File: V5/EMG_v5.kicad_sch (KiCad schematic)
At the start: 20 parts, among them J1 SJ1-3523N, J2 Output, U1 INA333xxDGK, U2 MCP6002-xP

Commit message: add power reference schematic block
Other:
- added sheet POWER_REFERENCE_BLOCK (POWER_REFERENCE_BLOCK.kicad_sch)
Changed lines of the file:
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@@
 		)
 		(instances
-			(project "EMG_v4"
+			(project "EMG_v5"
 				(path "/2c477672-822a-487d-bb83-204f5f41dbd8"
 					(reference "#PWR02")
@@
 		)
 		(instances
-			(project "EMG_v4"
+			(project "EMG_v5"
 				(path "/2c477672-822a-487d-bb83-204f5f41dbd8"
 					(reference "R6")
@@
 		)
 		(instances
-			(project "EMG_v4"
+			(project "EMG_v5"
 				(path "/2c477672-822a-487d-bb83-204f5f41dbd8"
 					(reference "R5")
@@
 		)
 		(instances
-			(project "EMG_v4"
+			(project "EMG_v5"
 				(path "/2c477672-822a-487d-bb83-204f5f41dbd8"
 					(reference "U2")
@@
 		)
 		(instances
-			(project "EMG_v4"
+			(project "EMG_v5"
 				(path "/2c477672-822a-487d-bb83-204f5f41dbd8"
 					(reference "Rg1")
@@
 		)
 		(instances
-			(project "EMG_v4"
+			(project "EMG_v5"
 				(path "/2c477672-822a-487d-bb83-204f5f41dbd8"
 					(reference "C2")
@@
 		)
 		(instances
-			(project "EMG_v4"
+			(project "EMG_v5"
 				(path "/2c477672-822a-487d-bb83-204f5f41dbd8"
 					(reference "R8")
@@
 		)
 		(instances
-			(project "EMG_v4"
+			(project "EMG_v5"
 				(path "/2c477672-822a-487d-bb83-204f5f41dbd8"
 					(reference "R3")
@@
 		)
 		(instances
-			(project "EMG_v4"
+			(project "EMG_v5"
 				(path "/2c477672-822a-487d-bb83-204f5f41dbd8"
 					(reference "R7")
@@
 		)
 		(instances
-			(project "EMG_v4"
+			(project "EMG_v5"
 				(path "/2c477672-822a-487d-bb83-204f5f41dbd8"
 					(reference "#FLG01")
@@
 		)
 		(instances
-			(project "EMG_v4"
+			(project "EMG_v5"
 				(path "/2c477672-822a-487d-bb83-204f5f41dbd8"
 					(reference "R2")
@@
 		)
 		(instances
-			(project "EMG_v4"
+			(project "EMG_v5"
 				(path "/2c477672-822a-487d-bb83-204f5f41dbd8"
 					(reference "U2")
@@
 		)
 		(instances
-			(project "EMG_v4"
+			(project "EMG_v5"
 				(path "/2c477672-822a-487d-bb83-204f5f41dbd8"
 					(reference "C6")
@@
 		)
 		(instances
-			(project "EMG_v4"
+			(project "EMG_v5"
 				(path "/2c477672-822a-487d-bb83-204f5f41dbd8"
 					(reference "R4")
@@
 		)
 		(instances
-			(project "EMG_v4"
+			(project "EMG_v5"
 				(path "/2c477672-822a-487d-bb83-204f5f41dbd8"
 					(reference "Rf1")
@@
 		)
 		(instances
-			(project "EMG_v4"
+			(project "EMG_v5"
 				(path "/2c477672-822a-487d-bb83-204f5f41dbd8"
 					(reference "#PWR01")
@@
 		)
 		(instances
-			(project "EMG_v4"
+			(project "EMG_v5"
 				(path "/2c477672-822a-487d-bb83-204f5f41dbd8"
 					(reference "J1")
@@
 		)
 		(instances
-			(project "EMG_v4"
+			(project "EMG_v5"
 				(path "/2c477672-822a-487d-bb83-204f5f41dbd8"
 					(reference "J2")
@@
 		)
 		(instances
-			(project "EMG_v4"
+			(project "EMG_v5"
 				(path "/2c477672-822a-487d-bb83-204f5f41dbd8"
 					(reference "C3")
@@
 		)
 		(instances
-			(project "EMG_v4"
+			(project "EMG_v5"
 				(path "/2c477672-822a-487d-bb83-204f5f41dbd8"
 					(reference "Cf2")
@@
 		)
 		(instances
-			(project "EMG_v4"
+			(project "EMG_v5"
 				(path "/2c477672-822a-487d-bb83-204f5f41dbd8"
 					(reference "U2")
@@
 		)
 		(instances
-			(project "EMG_v4"
+			(project "EMG_v5"
 				(path "/2c477672-822a-487d-bb83-204f5f41dbd8"
 					(reference "C4")
@@
 		)
 		(instances
-			(project "EMG_v4"
+			(project "EMG_v5"
 				(path "/2c477672-822a-487d-bb83-204f5f41dbd8"
 					(reference "C5")
@@
 		)
 		(instances
-			(project "EMG_v4"
+			(project "EMG_v5"
 				(path "/2c477672-822a-487d-bb83-204f5f41dbd8"
 					(reference "U1")
@@
 		)
 		(instances
-			(project "EMG_v4"
+			(project "EMG_v5"
 				(path "/2c477672-822a-487d-bb83-204f5f41dbd8"
 					(reference "Rg_HPF1")
@@
 		)
 		(instances
-			(project "EMG_v4"
+			(project "EMG_v5"
 				(path "/2c477672-822a-487d-bb83-204f5f41dbd8"
 					(reference "#FLG02")
@@
 				)
 			)
+		)
+	)
+	(sheet
+		(at 146.05 101.6)
+		(size 45.72 25.4)
+		(exclude_from_sim no)
+		(in_bom yes)
+		(on_board yes)
+		(dnp no)
+		(fields_autoplaced yes)
+		(stroke
+			(width 0.1524)
+			(type solid)
+		)
+		(fill
+			(color 0 0 0 0)
+		)
+		(property "Sheetname" "POWER_REFERENCE_BLOCK"
+			(at 146.05 100.8888 0)
+			(show_name no)
+			(do_not_autoplace no)
+			(effects
+				(font
+					(size 1.27 1.27)
+				)
+				(justify left bottom)
+			)
+		)
+		(property "Sheetfile" "POWER_REFERENCE_BLOCK.kicad_sch"
+			(at 146.05 127.6096 0)
+			(show_name no)
+			(do_not_autoplace no)
+			(effects
+				(font
+					(size 1.27 1.27)
+				)
+				(justify left top)
+			)
+		)
+		(instances
+			(project "EMG_v5"
+				(path "/4b7d3b9f-6eb5-4b2b-a72d-ec3d44a09101"
+					(page "2")
+				)
+			)

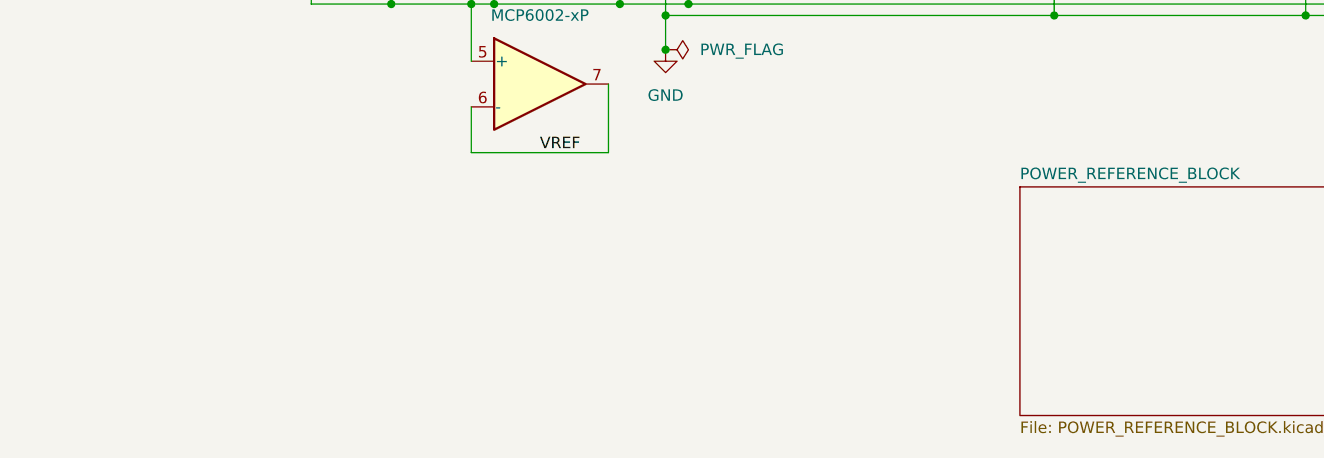
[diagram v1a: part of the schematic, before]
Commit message: add channel 1 analog schematic candidate
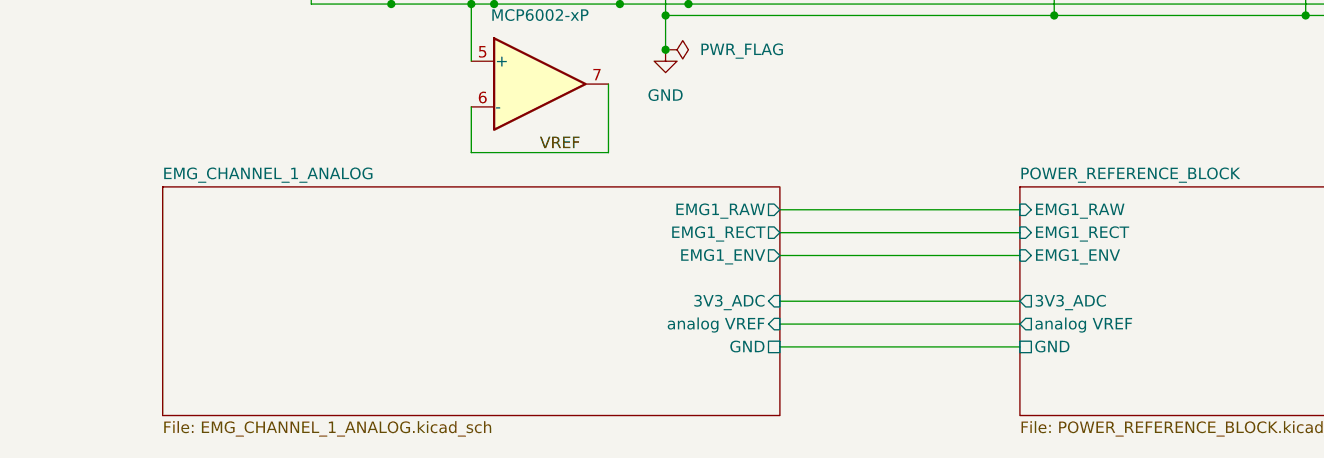
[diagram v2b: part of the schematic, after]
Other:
- added sheet EMG_CHANNEL_1_ANALOG (EMG_CHANNEL_1_ANALOG.kicad_sch)
- sheet POWER_REFERENCE_BLOCK ports: added 3V3_ADC, EMG1_ENV, EMG1_RAW, EMG1_RECT, GND, analog VREF; removed none
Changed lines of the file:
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@@
+			)
+		)
+		(pin "EMG1_RAW" input
+			(at 146.05 104.14 180)
+			(effects
+				(font
+					(size 1.27 1.27)
+				)
+				(justify left)
+			)
+		)
+		(pin "EMG1_RECT" input
+			(at 146.05 106.68 180)
+			(effects
+				(font
+					(size 1.27 1.27)
+				)
+				(justify left)
+			)
+		)
+		(pin "EMG1_ENV" input
+			(at 146.05 109.22 180)
+			(effects
+				(font
+					(size 1.27 1.27)
+				)
+				(justify left)
+			)
+		)
+		(pin "3V3_ADC" output
+			(at 146.05 114.3 180)
+			(effects
+				(font
+					(size 1.27 1.27)
+				)
+				(justify left)
+			)
+		)
+		(pin "analog VREF" output
+			(at 146.05 116.84 180)
+			(effects
+				(font
+					(size 1.27 1.27)
+				)
+				(justify left)
+			)
+		)
+		(pin "GND" passive
+			(at 146.05 119.38 180)
+			(effects
+				(font
+					(size 1.27 1.27)
+				)
+				(justify left)
 			)
 		)
@@
 				)
 			)
+		)
+	)
+	(wire
+		(pts
+			(xy 119.38 104.14) (xy 146.05 104.14)
+		)
+		(stroke
+			(width 0)
+			(type default)
+		)
+	)
+	(wire
+		(pts
+			(xy 119.38 106.68) (xy 146.05 106.68)
+		)
+		(stroke
+			(width 0)
+			(type default)
+		)
+	)
+	(wire
+		(pts
+			(xy 119.38 109.22) (xy 146.05 109.22)
+		)
+		(stroke
+			(width 0)
+			(type default)
+		)
+	)
+	(wire
+		(pts
+			(xy 119.38 114.3) (xy 146.05 114.3)
+		)
+		(stroke
+			(width 0)
+			(type default)
+		)
+	)
+	(wire
+		(pts
+			(xy 119.38 116.84) (xy 146.05 116.84)
+		)
+		(stroke
+			(width 0)
+			(type default)
+		)
+	)
+	(wire
+		(pts
+			(xy 119.38 119.38) (xy 146.05 119.38)
+		)
+		(stroke
+			(width 0)
+			(type default)
+		)
+	)
+	(sheet
+		(at 50.8 101.6)
+		(size 68.58 25.4)
+		(exclude_from_sim no)
+		(in_bom yes)
+		(on_board yes)
+		(dnp no)
+		(fields_autoplaced yes)
+		(stroke
+			(width 0.1524)
+			(type solid)
+		)
+		(fill
+			(color 0 0 0 0)
+		)
+		(property "Sheetname" "EMG_CHANNEL_1_ANALOG"
+			(at 50.8 100.8888 0)
+			(show_name no)
+			(do_not_autoplace no)
+			(effects
+				(font
+					(size 1.27 1.27)
+				)
+				(justify left bottom)
+			)
+		)
+		(property "Sheetfile" "EMG_CHANNEL_1_ANALOG.kicad_sch"
+			(at 50.8 127.6096 0)
+			(show_name no)
+			(do_not_autoplace no)
+			(effects
+				(font
+					(size 1.27 1.27)
+				)
+				(justify left top)
+			)
+		)
+		(pin "EMG1_RAW" output
+			(at 119.38 104.14 0)
+			(effects
+				(font
+					(size 1.27 1.27)
+				)
+				(justify right)
+			)
+		)
+		(pin "EMG1_RECT" output
+			(at 119.38 106.68 0)
+			(effects
+				(font
+					(size 1.27 1.27)
+				)
+				(justify right)
+			)
+		)
+		(pin "EMG1_ENV" output
+			(at 119.38 109.22 0)
+			(effects
+				(font
+					(size 1.27 1.27)
+				)
+				(justify right)
+			)
+		)
+		(pin "3V3_ADC" input
+			(at 119.38 114.3 0)
+			(effects
+				(font
+					(size 1.27 1.27)
+				)
+				(justify right)
+			)
+		)
+		(pin "analog VREF" input
+			(at 119.38 116.84 0)
+			(effects
+				(font
+					(size 1.27 1.27)
+				)
+				(justify right)
+			)
+		)
+		(pin "GND" passive
+			(at 119.38 119.38 0)
+			(effects
+				(font
+					(size 1.27 1.27)
+				)
+				(justify right)
+			)
+		)
+		(instances
+			(project "EMG_v5"
+				(path "/6a4b9db0-8b5f-4b75-9f44-83fd05e7b301"
+					(page "3")
+				)
+			)

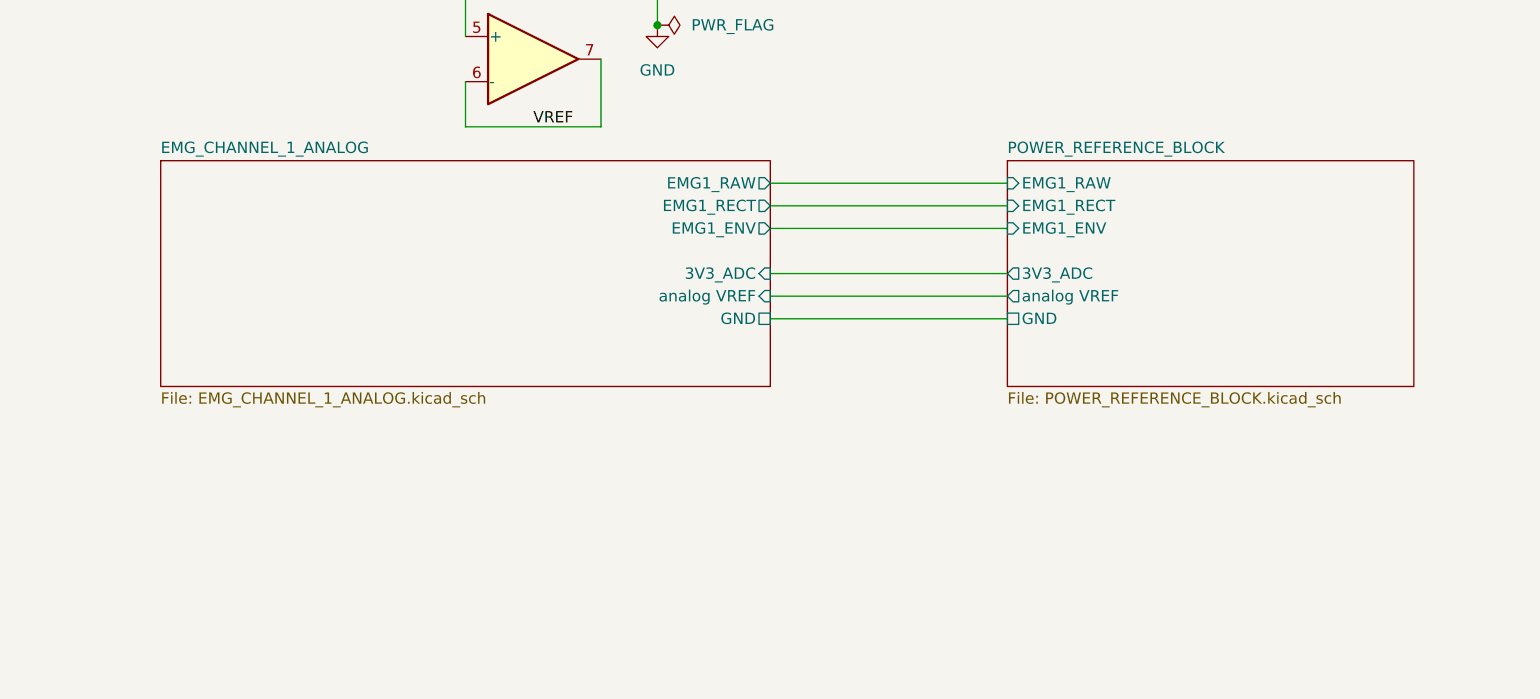
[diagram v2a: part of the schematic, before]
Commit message: implement channel 2 analog schematic
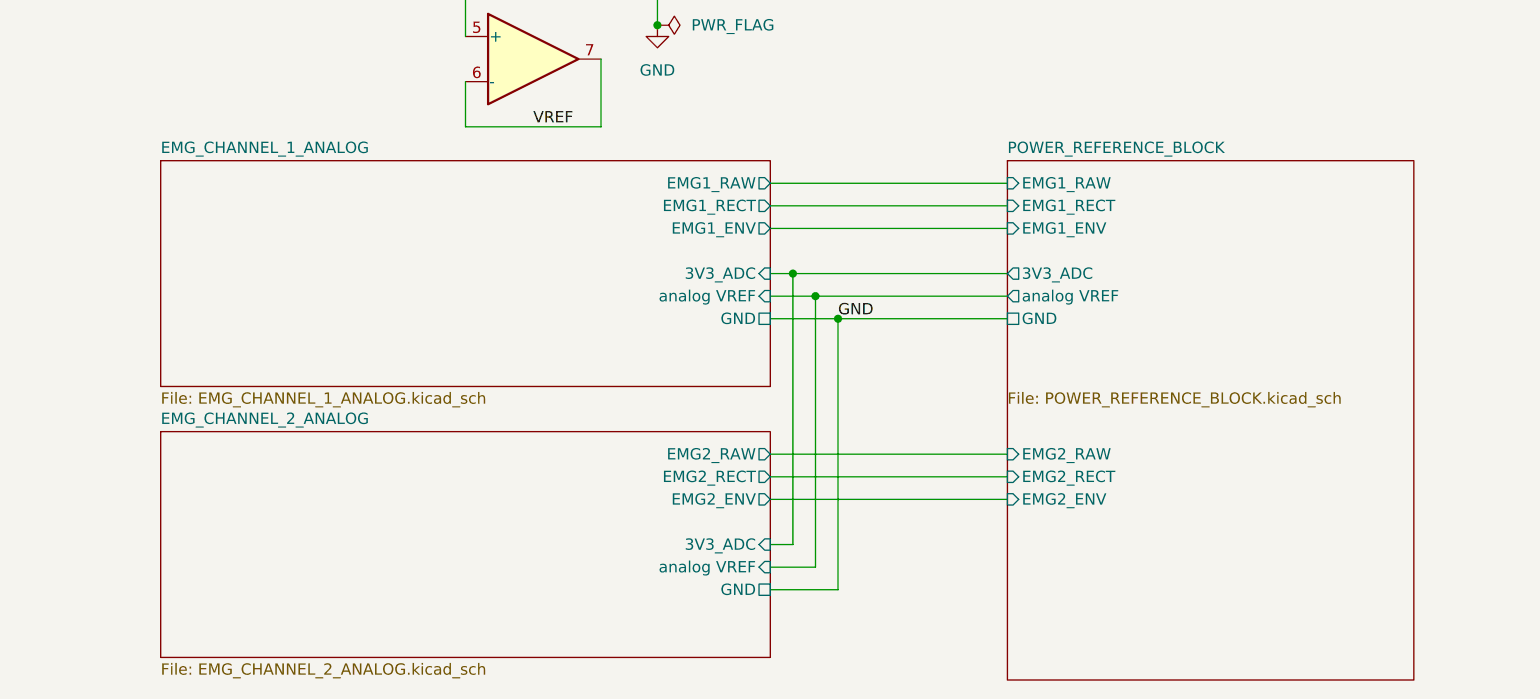
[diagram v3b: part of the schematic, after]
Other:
- added sheet EMG_CHANNEL_2_ANALOG (EMG_CHANNEL_2_ANALOG.kicad_sch)
- sheet POWER_REFERENCE_BLOCK ports: added EMG2_ENV, EMG2_RAW, EMG2_RECT; removed none
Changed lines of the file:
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@@
 	(sheet
 		(at 146.05 101.6)
-		(size 45.72 25.4)
+		(size 45.72 58.42)
 		(exclude_from_sim no)
 		(in_bom yes)
@@
 		(pin "EMG1_ENV" input
 			(at 146.05 109.22 180)
+			(effects
+				(font
+					(size 1.27 1.27)
+				)
+				(justify left)
+			)
+		)
+		(pin "EMG2_RAW" input
+			(at 146.05 134.62 180)
+			(effects
+				(font
+					(size 1.27 1.27)
+				)
+				(justify left)
+			)
+		)
+		(pin "EMG2_RECT" input
+			(at 146.05 137.16 180)
+			(effects
+				(font
+					(size 1.27 1.27)
+				)
+				(justify left)
+			)
+		)
+		(pin "EMG2_ENV" input
+			(at 146.05 139.7 180)
 			(effects
 				(font
@@
 				)
 			)
+		)
+	)
+	(wire
+		(pts
+			(xy 119.38 134.62) (xy 146.05 134.62)
+		)
+		(stroke
+			(width 0)
+			(type default)
+		)
+	)
+	(wire
+		(pts
+			(xy 119.38 137.16) (xy 146.05 137.16)
+		)
+		(stroke
+			(width 0)
+			(type default)
+		)
+	)
+	(wire
+		(pts
+			(xy 119.38 139.7) (xy 146.05 139.7)
+		)
+		(stroke
+			(width 0)
+			(type default)
+		)
+	)
+	(wire
+		(pts
+			(xy 119.38 144.78) (xy 121.92 144.78)
+		)
+		(stroke
+			(width 0)
+			(type default)
+		)
+	)
+	(wire
+		(pts
+			(xy 121.92 144.78) (xy 121.92 114.3)
+		)
+		(stroke
+			(width 0)
+			(type default)
+		)
+	)
+	(wire
+		(pts
+			(xy 119.38 147.32) (xy 124.46 147.32)
+		)
+		(stroke
+			(width 0)
+			(type default)
+		)
+	)
+	(wire
+		(pts
+			(xy 124.46 147.32) (xy 124.46 116.84)
+		)
+		(stroke
+			(width 0)
+			(type default)
+		)
+	)
+	(wire
+		(pts
+			(xy 119.38 149.86) (xy 127 149.86)
+		)
+		(stroke
+			(width 0)
+			(type default)
+		)
+	)
+	(wire
+		(pts
+			(xy 127 149.86) (xy 127 119.38)
+		)
+		(stroke
+			(width 0)
+			(type default)
+		)
+	)
+	(junction
+		(at 121.92 114.3)
+		(diameter 0)
+		(color 0 0 0 0)
+	)
+	(junction
+		(at 124.46 116.84)
+		(diameter 0)
+		(color 0 0 0 0)
+	)
+	(junction
+		(at 127 119.38)
+		(diameter 0)
+		(color 0 0 0 0)
+	)
+	(label "GND"
+		(at 127 119.38 0)
+			(effects
+				(font
+					(size 1.27 1.27)
+				)
+				(justify left bottom)
+			)
+	)
+	(sheet
+		(at 50.8 132.08)
+		(size 68.58 25.4)
+		(exclude_from_sim no)
+		(in_bom yes)
+		(on_board yes)
+		(dnp no)
+		(fields_autoplaced yes)
+		(stroke
+			(width 0.1524)
+			(type solid)
+		)
+		(fill
+			(color 0 0 0 0)
+		)
+		(property "Sheetname" "EMG_CHANNEL_2_ANALOG"
+			(at 50.8 131.3688 0)
+			(show_name no)
+			(do_not_autoplace no)
+			(effects
+				(font
+					(size 1.27 1.27)
+				)
+				(justify left bottom)
+			)
+		)
+		(property "Sheetfile" "EMG_CHANNEL_2_ANALOG.kicad_sch"
+			(at 50.8 158.0896 0)
+			(show_name no)
+			(do_not_autoplace no)
+			(effects
+				(font
+					(size 1.27 1.27)
+				)
+				(justify left top)
+			)
+		)
+		(pin "EMG2_RAW" output
+			(at 119.38 134.62 0)
+			(effects
+				(font
+					(size 1.27 1.27)
+				)
+				(justify right)
+			)
+		)
+		(pin "EMG2_RECT" output
+			(at 119.38 137.16 0)
+			(effects
+				(font
+					(size 1.27 1.27)
+				)
+				(justify right)
+			)
+		)
+		(pin "EMG2_ENV" output
+			(at 119.38 139.7 0)
+			(effects
+				(font
+					(size 1.27 1.27)
+				)
+				(justify right)
+			)
+		)
+		(pin "3V3_ADC" input
+			(at 119.38 144.78 0)
+			(effects
+				(font
+					(size 1.27 1.27)
+				)
+				(justify right)
+			)
+		)
+		(pin "analog VREF" input
+			(at 119.38 147.32 0)
+			(effects
+				(font
+					(size 1.27 1.27)
+				)
+				(justify right)
+			)
+		)
+		(pin "GND" passive
+			(at 119.38 149.86 0)
+			(effects
+				(font
+					(size 1.27 1.27)
+				)
+				(justify right)
+			)
+		)
+		(instances
+			(project "EMG_v5"
+				(path "/daafd134-eb58-4fde-8e0b-ae901f016f45"
+					(page "4")
+				)
+			)
